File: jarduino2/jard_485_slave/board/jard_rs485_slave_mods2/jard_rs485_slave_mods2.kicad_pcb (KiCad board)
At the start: 2 copper layers, 79.2 x 30 mm, 43 parts, among them J1 POWER, J3 Débit, J4 Niveaux, J6 EV1, Q4 BPC_FMMT38C, Q6 P03P4L-04, U1 BPC_Mod485, U6 BPC_DHT22

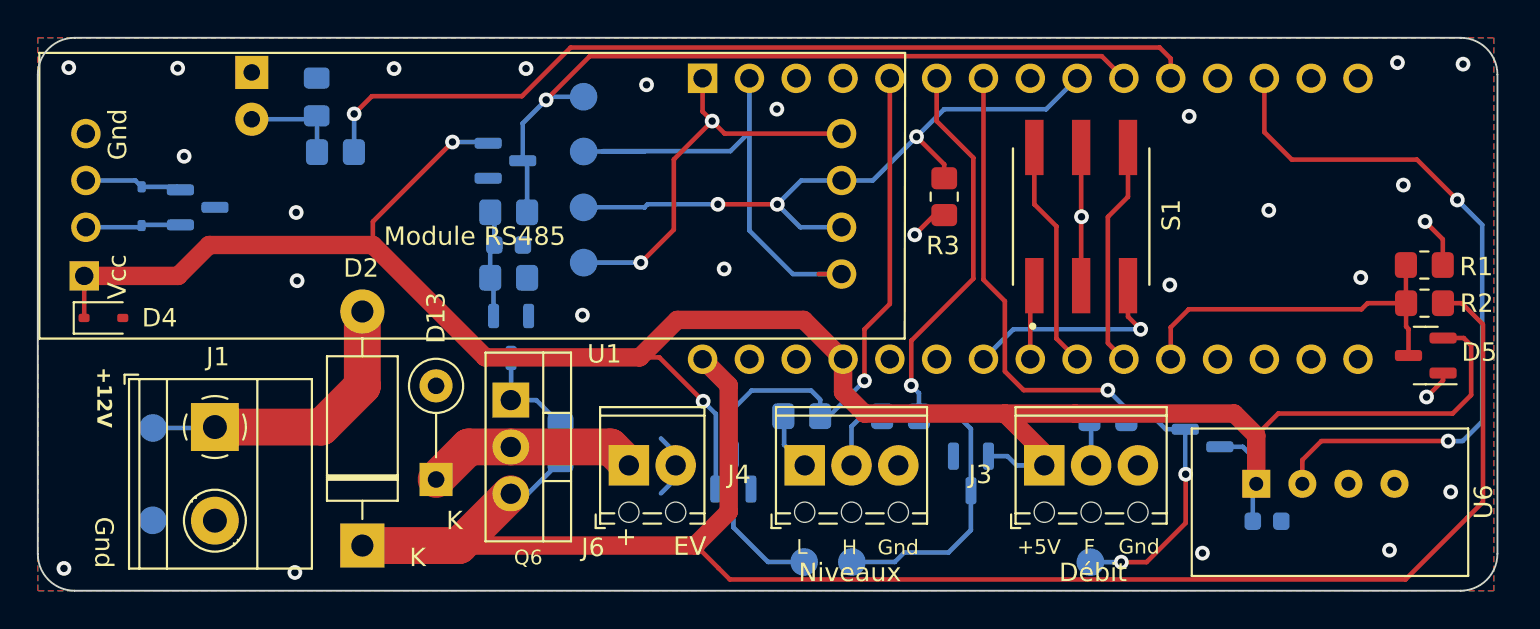
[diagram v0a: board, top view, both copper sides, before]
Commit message: Suppression du module RS485 et remplacement par le CI MAX485E lui-même. Preparation version G...
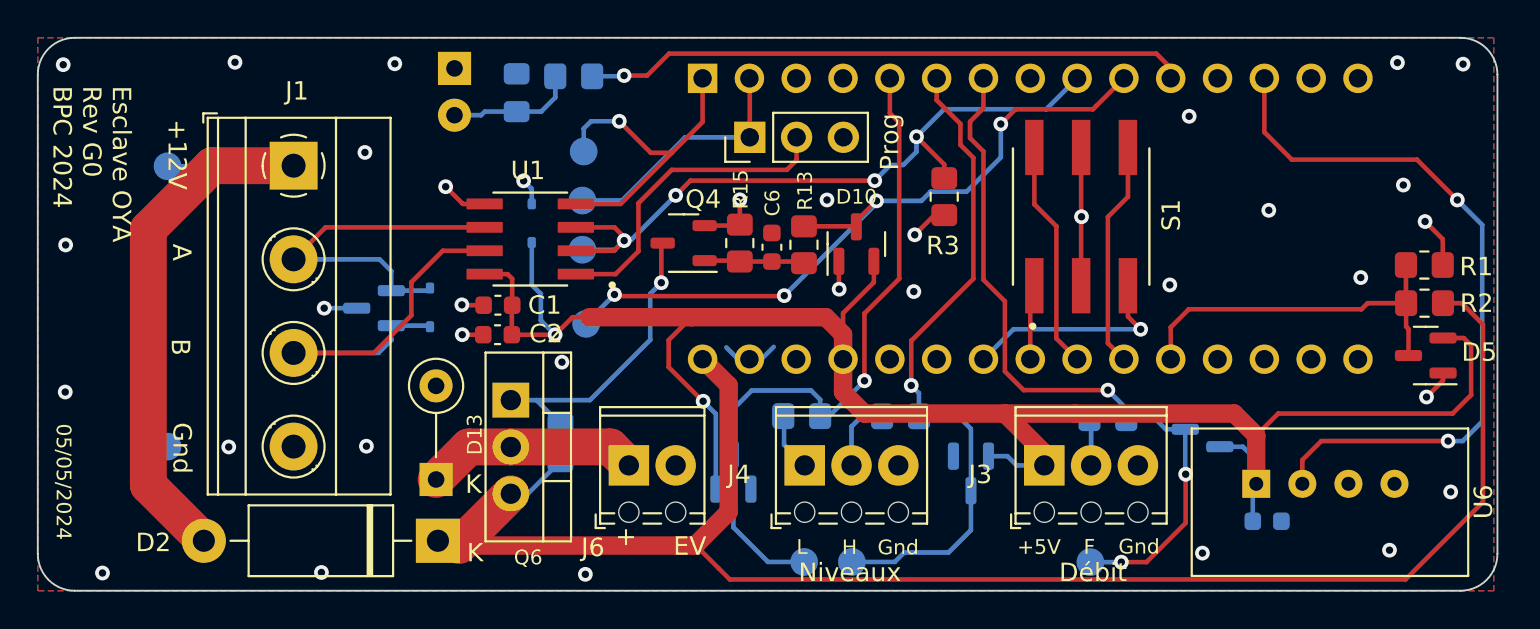
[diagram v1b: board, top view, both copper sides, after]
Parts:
- added C1: 100nF, Capacitor_SMD:C_0603_1608Metric, F.Cu at (138.4, 101.3)
- added C2: 1nF, Capacitor_SMD:C_0603_1608Metric, F.Cu at (138.3, 102.9)
- added JP2: Prog, Connector_PinHeader_2.54mm:PinHeader_1x03_P2.54mm_Vertical, F.Cu at (152.0, 92.2)
- C6, D10, Q4, R13, R15: moved to F.Cu
- D4: moved to B.Cu
- J1: footprint TerminalBlock_Phoenix:TerminalBlock_Phoenix_MKDS-1,5-2-5.08_1x02_P5.08mm_Horizontal -> TerminalBlock_Phoenix:TerminalBlock_Phoenix_MKDS-1,5-4-5.08_1x04_P5.08mm_Horizontal
- U1: value BPC_Mod485 -> MAX485E; footprint bpc:BPC_Mod485 -> bpc:BPC_MAX485E_SOIC127P600X175-8N
- moved U1 24.2 mm to (140.1, 97.7), turned to 180 degrees
- moved D4 23.8 mm to (140.2, 96.9), turned to 90 degrees
- moved D10 19.6 mm to (157.8, 98.0), turned to 90 degrees
- moved D11 16.6 mm to (134.7, 101.4), turned to -90 degrees
- moved R13 16.1 mm to (155.0, 98.0), turned to -90 degrees
- moved J1 14.8 mm to (127.3, 93.7)
- moved C6 14.3 mm to (153.2, 98.2), turned to 90 degrees
- moved TP2 14.2 mm to (120.4, 93.8)
- moved R12 13.6 mm to (142.5, 88.9)
- moved R15 12.7 mm to (151.5, 97.9), turned to 90 degrees
- moved TP15 12.3 mm to (143.1, 102.3)
- moved D9 11.0 mm to (131.6, 101.5), turned to 180 degrees
- moved D3 11.0 mm to (136.0, 88.5)
- moved D1 10.8 mm to (139.4, 89.8)
- moved Q4 10.7 mm to (148.4, 97.9), turned to 180 degrees
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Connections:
- D11 pad 1: BUS_B -> BUS_A
- D11 pad 2: BUS_A -> BUS_B
- D9 pad 1: BUS_B -> BUS_A
- D9 pad 2: BUS_A -> BUS_B
- J1 pad 2: GND -> BUS_A
- TP1 pad 1: TX -> RX
- TP3 pad 1: RX -> TX
- U1 pad 1: +5V -> Net-(JP2-C)
- U1 pad 2: BUS_B -> TX_EN
- U1 pad 3: BUS_A -> TX_EN
- U1 pad 4: GND -> TX
- U1 pad 5: TX -> GND
- U1 pad 6: TX_EN -> BUS_A
- U1 pad 7: TX_EN -> BUS_B
- U1 pad 8: RX -> +5V
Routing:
- net +5V: track 124.6 -> 103.2 mm
- net Net-(D2-A): track 16.4 -> 34.3 mm
- net Net-(JP2-C): track 0.00 -> 17.3 mm
- net BUS_B: track 5.18 -> 22.2 mm
- net LED: track 49.2 -> 32.8 mm
- net BUS_A: track 5.34 -> 19.9 mm
- net RX: track 27.2 -> 13.7 mm
- net GND: track 17.6 -> 29.9 mm, vias 27 -> 35
- net Net-(Q4-C): track 5.53 -> 16.3 mm, vias 0 -> 1
- net POWER_12V: track 94.4 -> 89.2 mm
- net TX: track 22.2 -> 18.0 mm, vias 2 -> 1
- net TX_EN: track 36.8 -> 40.0 mm, vias 3 -> 4
- net Net-(D1-A): track 5.57 -> 7.02 mm
- net CMD_EV1: track 41.7 -> 40.3 mm, vias 1 -> 4
- net FLOW: track 38.9 -> 39.5 mm
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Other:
- board text added: "05/05/2024"
- board text added: "A"
- board text added: "B"
- board text added: "Esclave OYA Rev G0 BPC 2024"
- board text added: "Prog"
- board text removed: "04/05/2024"
- board text removed: "Esclave OYA Rev F0 BPC 2024"
